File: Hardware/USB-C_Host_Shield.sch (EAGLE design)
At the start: 45 parts, among them J1 USB-C, J2 GPIN, J3 GPOUT, U1 ARDUINO_UNO_R3_SHIELDBASIC, U2 LM1117, U3 74HC4050, U5 MAX3421, U6 3.3V/150mA, Y1 12.0mhZ

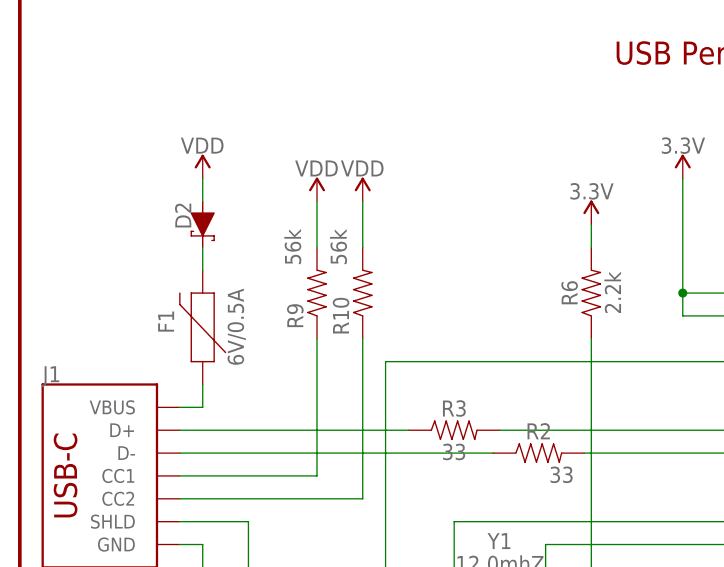
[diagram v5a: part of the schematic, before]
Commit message: Added product ID to R9 and R10
Created new part in Sparkle for this 56k 0603 resistor that is already input. The new ID, RES-17211, was added to the part and going to be add to the SparkFun parts library after project is verified with components and all
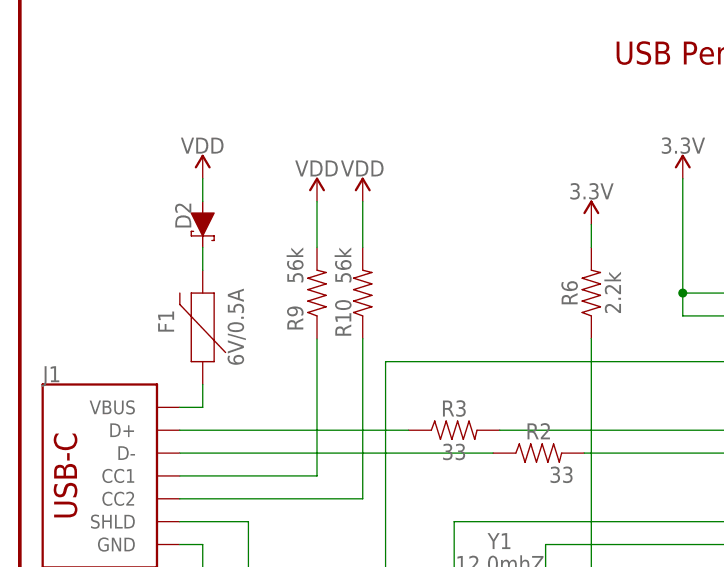
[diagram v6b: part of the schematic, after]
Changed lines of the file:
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@@
 <part name="JP1" library="SparkFun-Jumpers" deviceset="JUMPER-SMT_2_NC_TRACE" device="_SILK" package3d_urn="urn:adsk.eagle:package:39281/1"/>
 <part name="S1" library="SparkFun-Switches" deviceset="SWITCH-SPDT" device="-SMD-AYZ0202" value="Main Power"/>
-<part name="R9" library="SparkFun-Resistors" deviceset="56KOHM" device="" value="56k"/>
-<part name="R10" library="SparkFun-Resistors" deviceset="56KOHM" device="" value="56k"/>
 <part name="SUPPLY3" library="SparkFun-PowerSymbols" deviceset="VDD" device=""/>
 <part name="SUPPLY12" library="SparkFun-PowerSymbols" deviceset="VDD" device=""/>
@@
 <part name="S3" library="SparkFun-Switches" deviceset="SWITCH-SPDT" device="-SMD-AYZ0202" value="Power Select"/>
 <part name="SUPPLY11" library="SparkFun-PowerSymbols" deviceset="VDD" device=""/>
+<part name="R9" library="SparkFun-Resistors" deviceset="56KOHM" device="" value="56k"/>
+<part name="R10" library="SparkFun-Resistors" deviceset="56KOHM" device="" value="56k"/>
 </parts>
 <sheets>
@@
 <attribute name="VALUE" x="109.22" y="160.274" size="1.778" layer="96" font="vector" align="top-center"/>
 </instance>
-<instance part="R9" gate="G$1" x="33.02" y="78.74" smashed="yes" rot="R90">
-<attribute name="NAME" x="31.496" y="76.2" size="1.778" layer="95" font="vector" rot="R90" align="bottom-center"/>
-<attribute name="VALUE" x="29.464" y="83.82" size="1.778" layer="96" font="vector" rot="R90" align="top-center"/>
-</instance>
-<instance part="R10" gate="G$1" x="38.1" y="78.74" smashed="yes" rot="R90">
-<attribute name="NAME" x="36.576" y="76.2" size="1.778" layer="95" font="vector" rot="R90" align="bottom-center"/>
-<attribute name="VALUE" x="34.544" y="83.82" size="1.778" layer="96" font="vector" rot="R90" align="top-center"/>
-</instance>
 <instance part="SUPPLY3" gate="VDD" x="20.32" y="91.44" smashed="yes">
 <attribute name="VALUE" x="20.32" y="94.234" size="1.778" layer="96" font="vector" align="bottom-center"/>
@@
 <instance part="SUPPLY11" gate="VDD" x="98.298" y="160.274" smashed="yes">
 <attribute name="VALUE" x="98.298" y="163.068" size="1.778" layer="96" font="vector" align="bottom-center"/>
+</instance>
+<instance part="R9" gate="G$1" x="33.02" y="78.74" smashed="yes" rot="R90">
+<attribute name="NAME" x="31.496" y="75.946" size="1.778" layer="95" font="vector" rot="R90" align="bottom-center"/>
+<attribute name="VALUE" x="29.718" y="81.788" size="1.778" layer="96" font="vector" rot="R90" align="top-center"/>
+</instance>
+<instance part="R10" gate="G$1" x="38.1" y="78.74" smashed="yes" rot="R90">
+<attribute name="NAME" x="36.83" y="75.946" size="1.778" layer="95" font="vector" rot="R90" align="bottom-center"/>
+<attribute name="VALUE" x="35.052" y="81.788" size="1.778" layer="96" font="vector" rot="R90" align="top-center"/>
 </instance>
 </instances>
@@
 <pinref part="J1" gate="J1" pin="CC1"/>
 <wire x1="17.78" y1="58.42" x2="33.02" y2="58.42" width="0.1524" layer="91"/>
+<wire x1="33.02" y1="58.42" x2="33.02" y2="73.66" width="0.1524" layer="91"/>
 <pinref part="R9" gate="G$1" pin="1"/>
-<wire x1="33.02" y1="58.42" x2="33.02" y2="73.66" width="0.1524" layer="91"/>
 </segment>
 </net>
@@
 <pinref part="J1" gate="J1" pin="CC2"/>
 <wire x1="17.78" y1="55.88" x2="38.1" y2="55.88" width="0.1524" layer="91"/>
+<wire x1="38.1" y1="55.88" x2="38.1" y2="73.66" width="0.1524" layer="91"/>
 <pinref part="R10" gate="G$1" pin="1"/>
-<wire x1="38.1" y1="55.88" x2="38.1" y2="73.66" width="0.1524" layer="91"/>
 </segment>
 </net>
@@
 <net name="VDD" class="0">
 <segment>
-<pinref part="R9" gate="G$1" pin="2"/>
 <wire x1="33.02" y1="83.82" x2="33.02" y2="88.9" width="0.1524" layer="91"/>
 <pinref part="SUPPLY12" gate="VDD" pin="VDD"/>
-</segment>
-<segment>
-<pinref part="R10" gate="G$1" pin="2"/>
+<pinref part="R9" gate="G$1" pin="2"/>
+</segment>
+<segment>
 <wire x1="38.1" y1="83.82" x2="38.1" y2="88.9" width="0.1524" layer="91"/>
 <pinref part="SUPPLY13" gate="VDD" pin="VDD"/>
-</segment>
-<segment>
+<pinref part="R10" gate="G$1" pin="2"/>
+</segment>
+<segment>

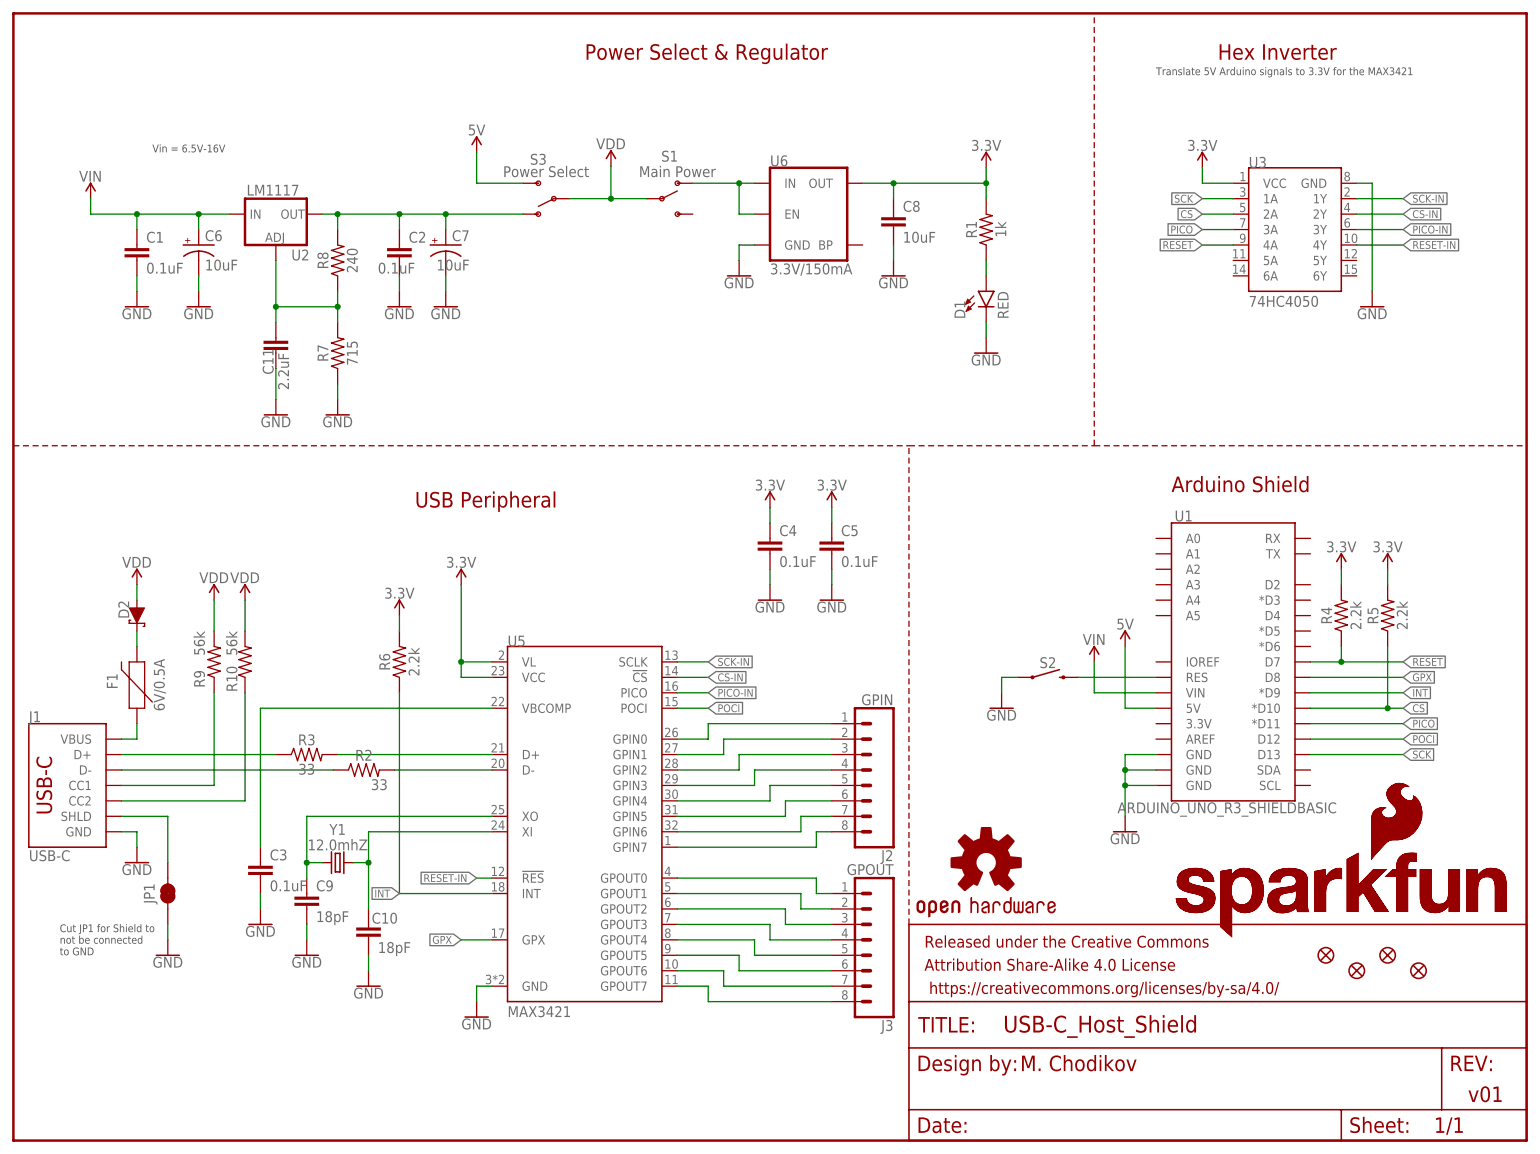
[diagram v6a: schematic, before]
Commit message: Updated board for design review
Updated for design review notes - primarily updating the Arduino shield with buzzard labels, adjusting components to have description, adjusting VDD to have the input after the main power switch, include the original designer, and adjusting label location for the power switches.
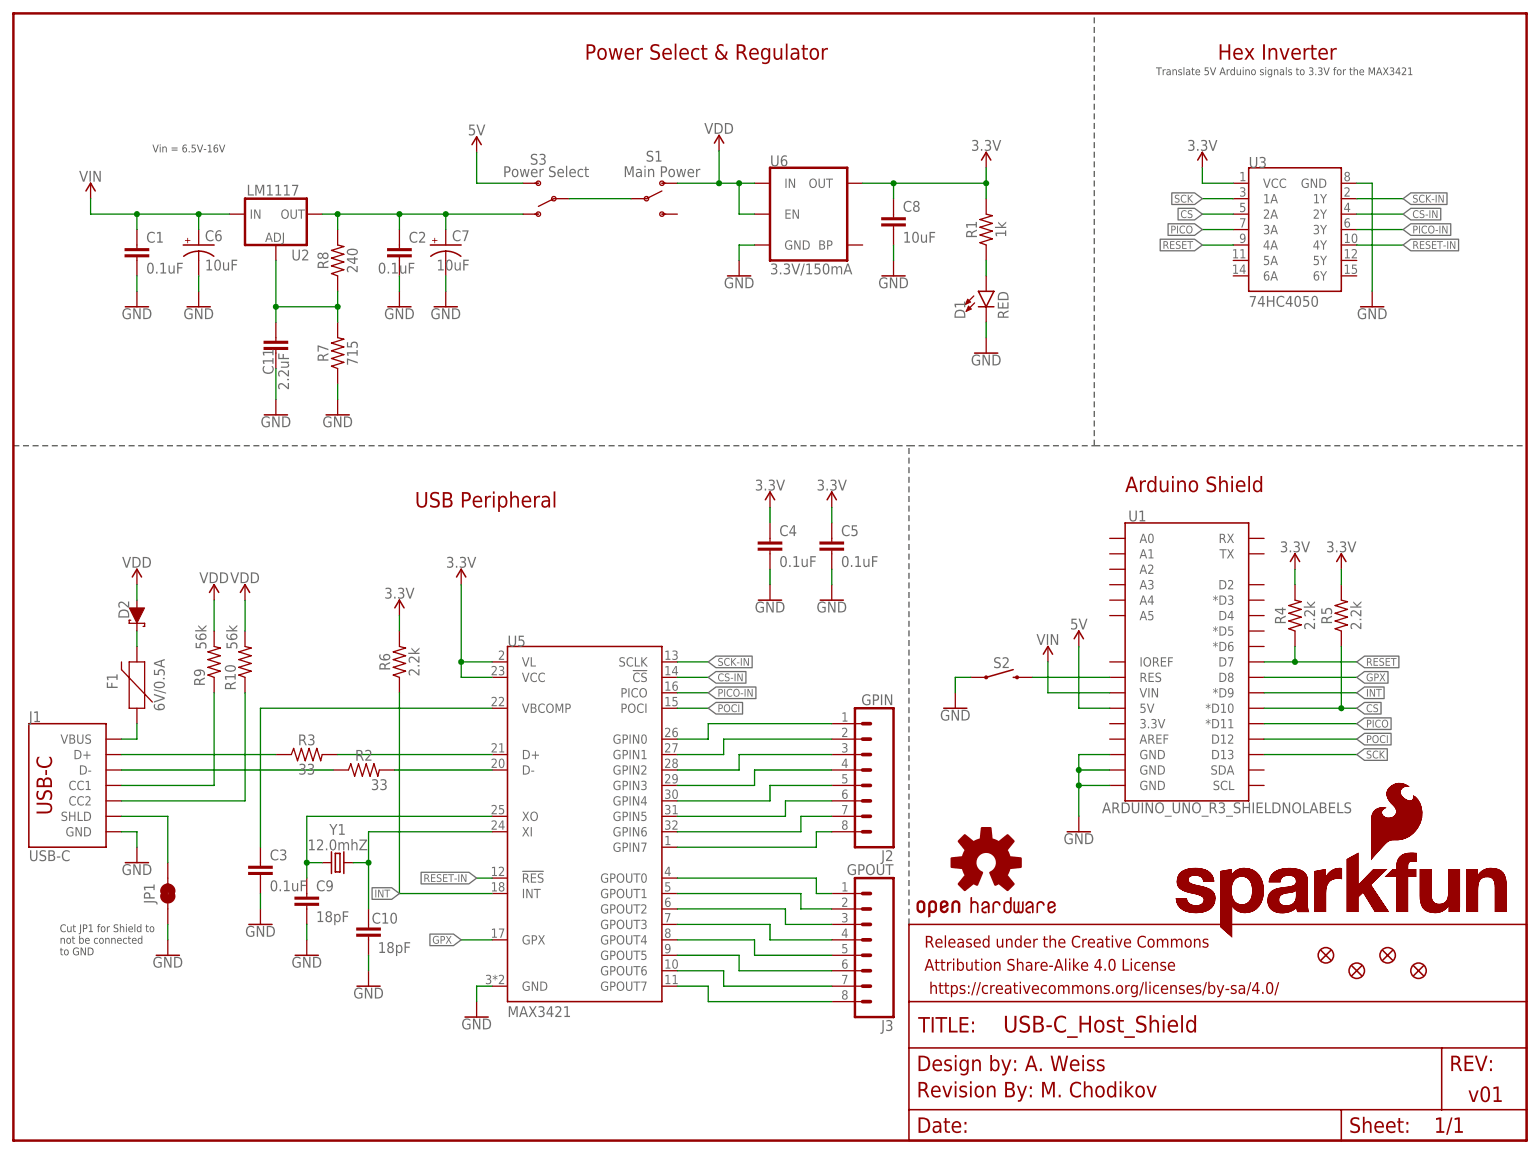
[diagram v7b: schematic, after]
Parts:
- added LOGO7: REVISION, SparkFun-Aesthetics:REVISION
- U1: value ARDUINO_UNO_R3_SHIELDBASIC -> ARDUINO_UNO_R3_SHIELDNOLABELS; device SparkFun-Boards:ARDUINO_UNO_R3_SHIELDBASIC -> SparkFun-Boards:ARDUINO_UNO_R3_SHIELDNOLABELS
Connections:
- removed net POWER_IN: S1.O, U6.EN, U6.IN
- new net N$2: S1.P, S3.P
- net VDD: now also S1.O, U6.EN, U6.IN; no longer S1.P, S3.P
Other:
- note added: "A. Weiss"
- moved on the sheet: R4, R5, S1, S2, U1

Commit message: Updates to layout as per Design review notes
Updates to notation in schematic, adjusted routing for better GND pour connections
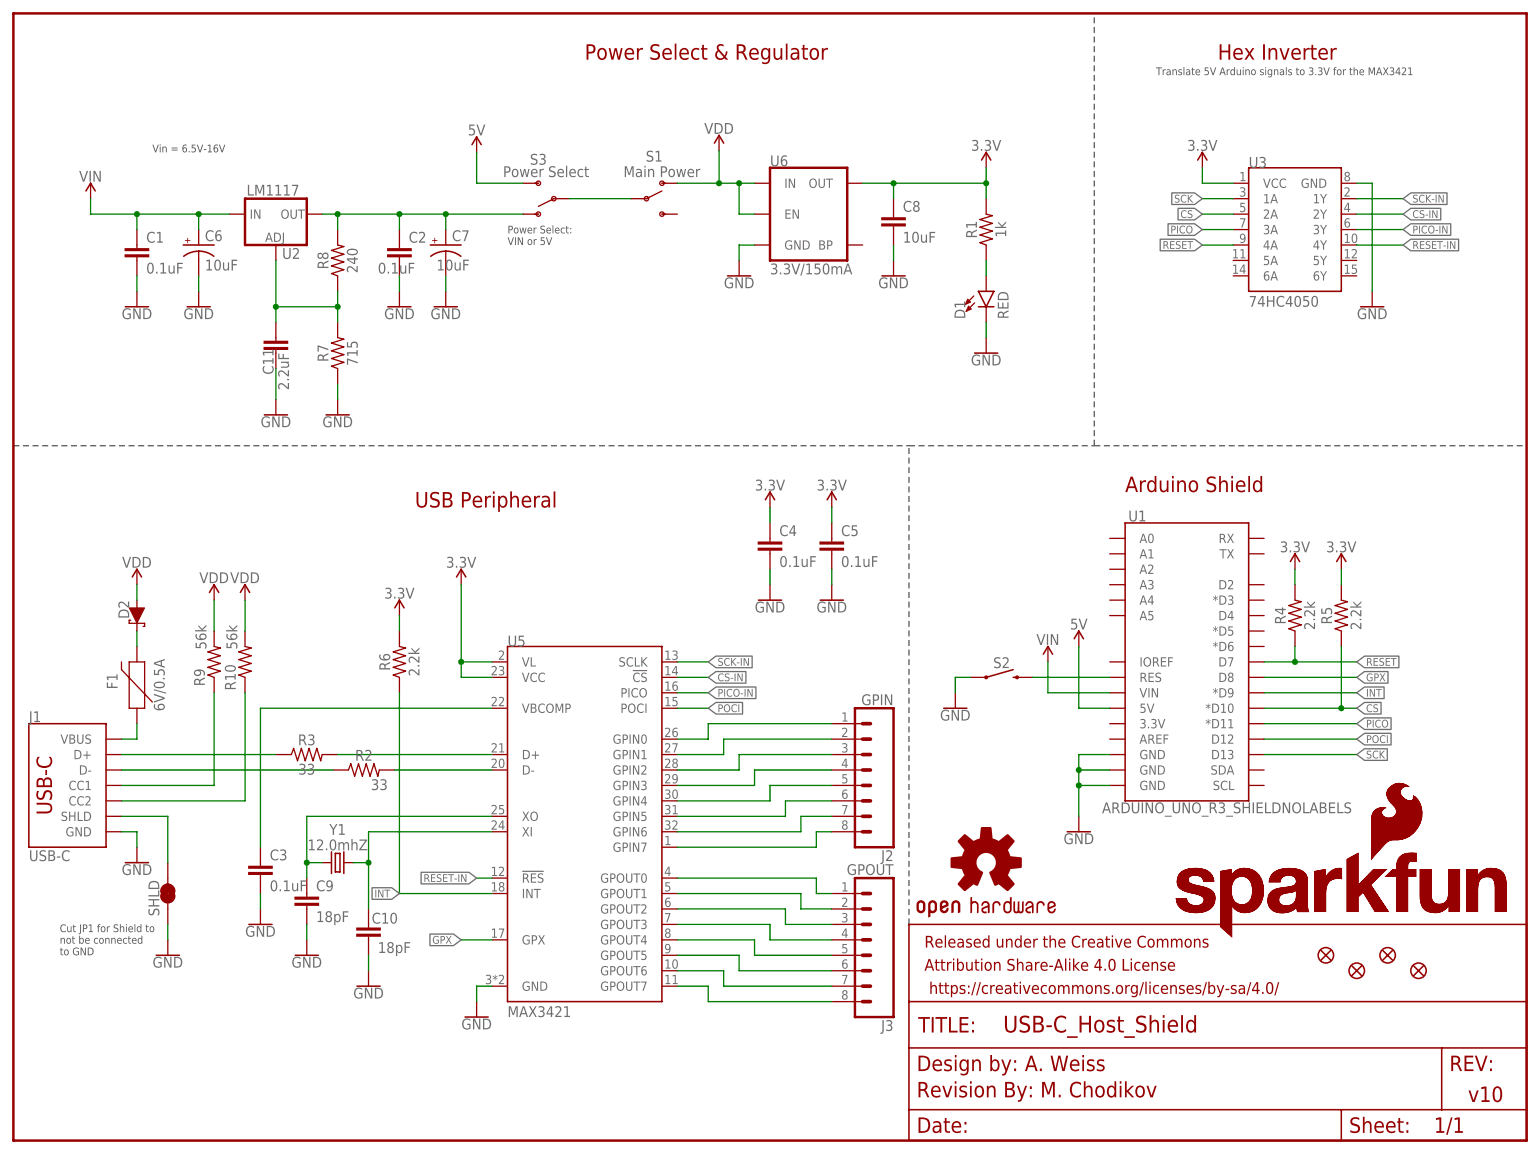
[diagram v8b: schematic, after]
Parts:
- renumbered JP1 to SHLD
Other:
- note added: "Power Select: VIN or 5V"
- note added: "v10"
- note removed: "v01"
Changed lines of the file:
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@@
 <part name="SUPPLY9" library="SparkFun-PowerSymbols" deviceset="VIN" device=""/>
 <part name="GND16" library="SparkFun-PowerSymbols" deviceset="GND" device=""/>
-<part name="JP1" library="SparkFun-Jumpers" deviceset="JUMPER-SMT_2_NC_TRACE" device="_SILK" package3d_urn="urn:adsk.eagle:package:39281/1"/>
+<part name="SHLD" library="SparkFun-Jumpers" deviceset="JUMPER-SMT_2_NC_TRACE" device="_SILK" package3d_urn="urn:adsk.eagle:package:39281/1"/>
 <part name="S1" library="SparkFun-Switches" deviceset="SWITCH-SPDT" device="-SMD-AYZ0202" value="Main Power"/>
 <part name="SUPPLY3" library="SparkFun-PowerSymbols" deviceset="VDD" device=""/>
@@
 <plain>
 <text x="168.91" y="7.112" size="2.54" layer="94" font="vector">M. Chodikov</text>
-<text x="239.268" y="6.35" size="2.54" layer="94" font="vector">v01</text>
+<text x="239.268" y="6.35" size="2.54" layer="94" font="vector">v10</text>
 <text x="93.98" y="177.8" size="2.54" layer="94" font="vector">Power Select &amp; Regulator</text>
 <text x="182.88" y="106.68" size="2.54" layer="94" font="vector">Arduino Shield</text>
@@
 to GND</text>
 <text x="166.37" y="11.43" size="2.54" layer="94" font="vector">A. Weiss</text>
+<text x="81.28" y="147.32" size="1.27" layer="97" font="vector">Power Select:
+VIN or 5V</text>
 </plain>
 <instances>
@@
 </instance>
 <instance part="U2" gate="G$1" x="43.18" y="152.4" smashed="yes">
-<attribute name="NAME" x="45.72" y="144.78" size="1.778" layer="95"/>
+<attribute name="NAME" x="44.196" y="145.034" size="1.778" layer="95" font="vector"/>
 <attribute name="VALUE" x="38.354" y="155.448" size="1.778" layer="96" font="vector"/>
 </instance>
@@
 <attribute name="VALUE" x="25.4" y="30.226" size="1.778" layer="96" font="vector" align="top-center"/>
 </instance>
-<instance part="JP1" gate="G$1" x="25.4" y="40.64" smashed="yes" rot="R90">
-<attribute name="NAME" x="22.352" y="40.64" size="1.778" layer="95" font="vector" rot="R90" align="center"/>
+<instance part="SHLD" gate="G$1" x="25.4" y="40.64" smashed="yes" rot="R90">
+<attribute name="NAME" x="23.114" y="39.878" size="1.778" layer="95" font="vector" rot="R90" align="center"/>
 <attribute name="VALUE" x="28.448" y="40.64" size="1.778" layer="96" font="vector" rot="R90" align="center" display="off"/>
 </instance>
@@
 <wire x1="25.4" y1="35.56" x2="25.4" y2="33.02" width="0.1524" layer="91"/>
 <pinref part="GND16" gate="1" pin="GND"/>
-<pinref part="JP1" gate="G$1" pin="1"/>
+<pinref part="SHLD" gate="G$1" pin="1"/>
 </segment>
 <segment>
@@
 <wire x1="17.78" y1="53.34" x2="25.4" y2="53.34" width="0.1524" layer="91"/>
 <wire x1="25.4" y1="53.34" x2="25.4" y2="45.72" width="0.1524" layer="91"/>
-<pinref part="JP1" gate="G$1" pin="2"/>
-</segment>
-</net>
+<pinref part="SHLD" gate="G$1" pin="2"/>
+</segment>
+</net>
